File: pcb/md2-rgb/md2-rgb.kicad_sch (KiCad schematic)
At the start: 19 parts, among them J101 MD-90SM, J102 MD-90SM

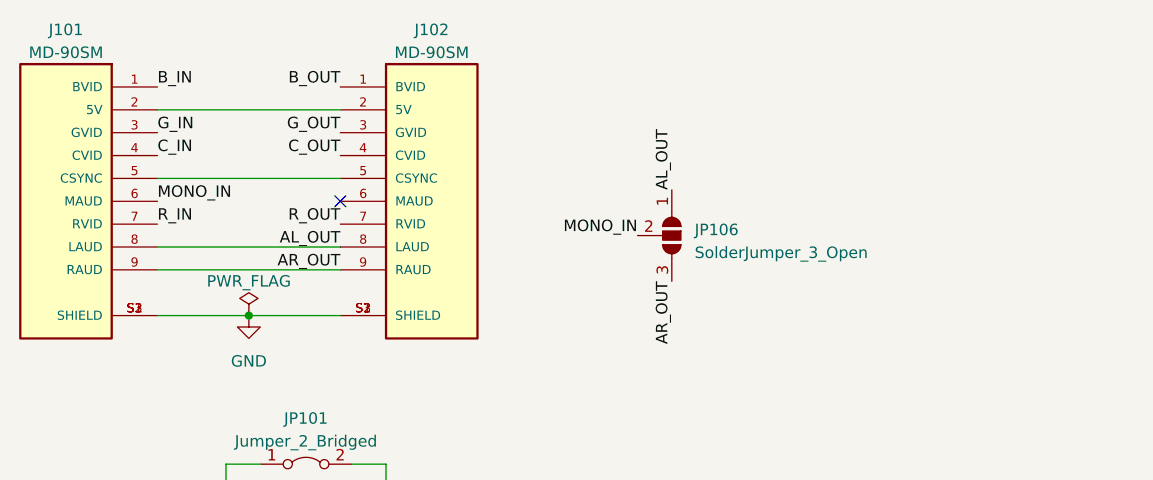
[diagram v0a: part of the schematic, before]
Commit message: Adds FPC to RGB breakout
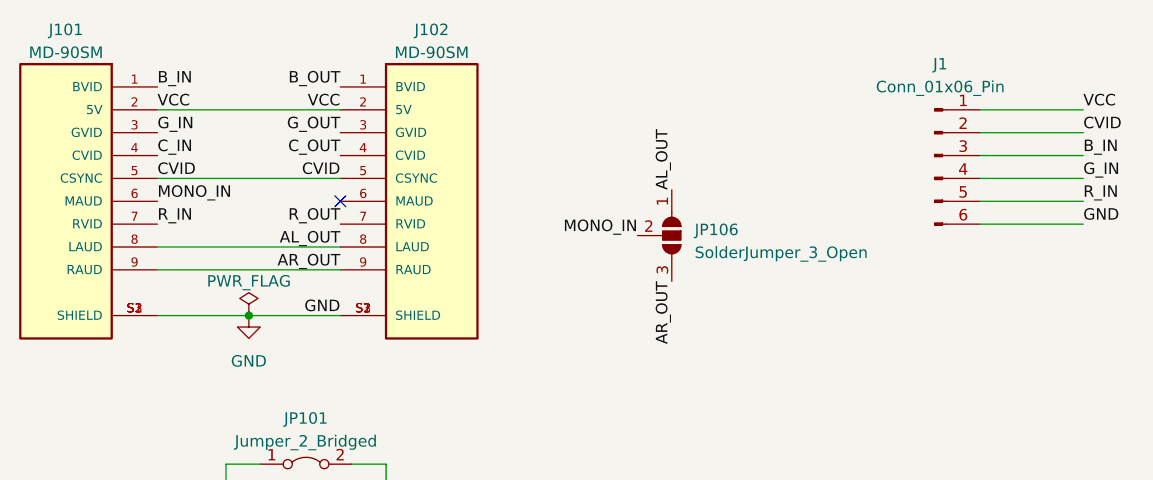
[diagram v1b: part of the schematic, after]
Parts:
- added J1: Conn_01x06_Pin, Connector_FFC-FPC:TE_0-1734839-6_1x06-1MP_P0.5mm_Horizontal, symbol Connector:Conn_01x06_Pin
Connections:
- net B_IN: now also J1.3 (Pin_3)
- net GND: now also J1.6 (Pin_6)
- net G_IN: now also J1.4 (Pin_4)
- net R_IN: now also J1.5 (Pin_5)
- net VCC: now reaches J101.2 (5V), J102.2 (5V)
- net VCC: now also J1.1 (Pin_1)
- net CVID: now reaches J101.5 (CSYNC), J102.5 (CSYNC)
- net CVID: now also J1.2 (Pin_2)
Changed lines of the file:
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@@
+    (stroke (width 0) (type default))
+  )
+  (wire (pts (xy 143.51 30.48) (xy 132.08 30.48))
+    (stroke (width 0) (type default))
+  )
+  (wire (pts (xy 143.51 38.1) (xy 132.08 38.1))
     (stroke (width 0) (type default))
   )
@@
     (stroke (width 0) (type default))
   )
+  (wire (pts (xy 143.51 43.18) (xy 132.08 43.18))
+    (stroke (width 0) (type default))
+  )
   (wire (pts (xy 62.23 134.62) (xy 66.04 134.62))
     (stroke (width 0) (type default))
   )
+  (wire (pts (xy 143.51 35.56) (xy 132.08 35.56))
+    (stroke (width 0) (type default))
+  )
   (wire (pts (xy 66.04 175.26) (xy 71.12 175.26))
     (stroke (width 0) (type default))
@@
     (stroke (width 0) (type default))
   )
+  (wire (pts (xy 143.51 33.02) (xy 132.08 33.02))
+    (stroke (width 0) (type default))
+  )
   (wire (pts (xy 48.26 110.49) (xy 50.8 110.49))
     (stroke (width 0) (type default))
@@
     (stroke (width 0) (type default))
   )
+  (wire (pts (xy 143.51 40.64) (xy 132.08 40.64))
+    (stroke (width 0) (type default))
+  )
   (wire (pts (xy 48.26 78.74) (xy 48.26 69.85))
     (stroke (width 0) (type default))
@@
     (effects (font (size 1.27 1.27)) (justify left bottom))
   )
+  (label "GND" (at 60.96 53.34 180) (fields_autoplaced)
+    (effects (font (size 1.27 1.27)) (justify right bottom))
+  )
   (label "AR_OUT" (at 97.79 49.53 270) (fields_autoplaced)
     (effects (font (size 1.27 1.27)) (justify right bottom))
   )
+  (label "VCC" (at 60.96 30.48 180) (fields_autoplaced)
+    (effects (font (size 1.27 1.27)) (justify right bottom))
+  )
   (label "B_IN" (at 44.45 143.51 180) (fields_autoplaced)
     (effects (font (size 1.27 1.27)) (justify right bottom))
@@
     (effects (font (size 1.27 1.27)) (justify right bottom))
   )
+  (label "B_IN" (at 143.51 35.56 0) (fields_autoplaced)
+    (effects (font (size 1.27 1.27)) (justify left bottom))
+  )
   (label "R_IN" (at 44.45 78.74 180) (fields_autoplaced)
     (effects (font (size 1.27 1.27)) (justify right bottom))
@@
     (effects (font (size 1.27 1.27)) (justify right bottom))
   )
+  (label "VCC" (at 143.51 30.48 0) (fields_autoplaced)
+    (effects (font (size 1.27 1.27)) (justify left bottom))
+  )
   (label "G_IN" (at 44.45 110.49 180) (fields_autoplaced)
     (effects (font (size 1.27 1.27)) (justify right bottom))
   )
+  (label "R_IN" (at 143.51 40.64 0) (fields_autoplaced)
+    (effects (font (size 1.27 1.27)) (justify left bottom))
+  )
   (label "MONO_IN" (at 40.64 40.64 0) (fields_autoplaced)
     (effects (font (size 1.27 1.27)) (justify left bottom))
@@
     (effects (font (size 1.27 1.27)) (justify left bottom))
   )
+  (label "CVID" (at 60.96 38.1 180) (fields_autoplaced)
+    (effects (font (size 1.27 1.27)) (justify right bottom))
+  )
   (label "G_OUT" (at 71.12 110.49 0) (fields_autoplaced)
     (effects (font (size 1.27 1.27)) (justify left bottom))
@@
     (effects (font (size 1.27 1.27)) (justify left bottom))
   )
+  (label "CVID" (at 40.64 38.1 0) (fields_autoplaced)
+    (effects (font (size 1.27 1.27)) (justify left bottom))
+  )
   (label "B_OUT" (at 60.96 27.94 180) (fields_autoplaced)
     (effects (font (size 1.27 1.27)) (justify right bottom))
   )
+  (label "GND" (at 143.51 43.18 0) (fields_autoplaced)
+    (effects (font (size 1.27 1.27)) (justify left bottom))
+  )
+  (label "CVID" (at 143.51 33.02 0) (fields_autoplaced)
+    (effects (font (size 1.27 1.27)) (justify left bottom))
+  )
+  (label "G_IN" (at 143.51 38.1 0) (fields_autoplaced)
+    (effects (font (size 1.27 1.27)) (justify left bottom))
+  )
   (label "C_OUT" (at 60.96 35.56 180) (fields_autoplaced)
     (effects (font (size 1.27 1.27)) (justify right bottom))
+  )
+  (label "VCC" (at 40.64 30.48 0) (fields_autoplaced)
+    (effects (font (size 1.27 1.27)) (justify left bottom))
   )
   (label "R_OUT" (at 60.96 43.18 180) (fields_autoplaced)
@@
         )
       )
+    )
+  )
+  (symbol (lib_id "Connector:Conn_01x06_Pin") (at 127 35.56 0) (unit 1)
+    (in_bom yes) (on_board yes) (dnp no) (fields_autoplaced)
+    (property "Reference" "J1" (at 127.635 25.4 0)
+      (effects (font (size 1.27 1.27)))
+    )
+    (property "Value" "Conn_01x06_Pin" (at 127.635 27.94 0)
+      (effects (font (size 1.27 1.27)))
+    )
+    (property "Footprint" "Connector_FFC-FPC:TE_0-1734839-6_1x06-1MP_P0.5mm_Horizontal" (at 127 35.56 0)
+      (effects (font (size 1.27 1.27)) hide)
+    )
+    (property "Datasheet" "~" (at 127 35.56 0)
+      (effects (font (size 1.27 1.27)) hide)
+    )
+    (pin "1")
+    (pin "2")
+    (pin "3")
+    (pin "4")
+    (pin "5")
+    (pin "6")
+    (instances
+      (project "md2-rgb"
+        (path "/8135f8d6-ea78-471e-a120-e2dd0a7eef29"
+          (reference "J1") (unit 1)
+        )
+      )

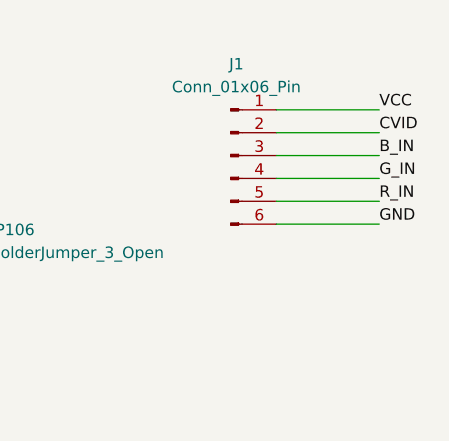
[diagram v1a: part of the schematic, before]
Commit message: Flips FFC
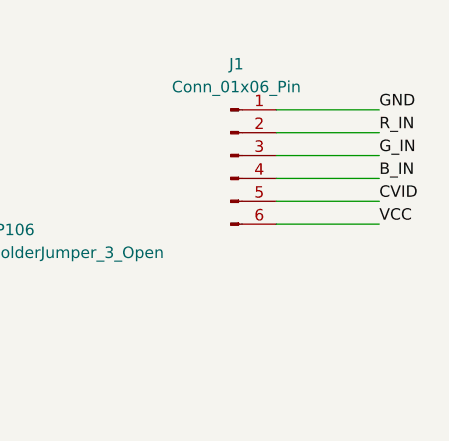
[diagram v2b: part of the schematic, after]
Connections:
- net B_IN: now also J1.4 (Pin_4); no longer J1.3 (Pin_3)
- net CVID: now also J1.5 (Pin_5); no longer J1.2 (Pin_2)
- net GND: now also J1.1 (Pin_1); no longer J1.6 (Pin_6)
- net G_IN: now also J1.3 (Pin_3); no longer J1.4 (Pin_4)
- net R_IN: now also J1.2 (Pin_2); no longer J1.5 (Pin_5)
- net VCC: now also J1.6 (Pin_6); no longer J1.1 (Pin_1)
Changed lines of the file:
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@@
     (effects (font (size 1.27 1.27)) (justify right bottom))
   )
-  (label "B_IN" (at 143.51 35.56 0) (fields_autoplaced)
+  (label "B_IN" (at 143.51 38.1 0) (fields_autoplaced)
     (effects (font (size 1.27 1.27)) (justify left bottom))
   )
@@
     (effects (font (size 1.27 1.27)) (justify right bottom))
   )
-  (label "VCC" (at 143.51 30.48 0) (fields_autoplaced)
+  (label "VCC" (at 143.51 43.18 0) (fields_autoplaced)
     (effects (font (size 1.27 1.27)) (justify left bottom))
   )
@@
     (effects (font (size 1.27 1.27)) (justify right bottom))
   )
-  (label "R_IN" (at 143.51 40.64 0) (fields_autoplaced)
+  (label "R_IN" (at 143.51 33.02 0) (fields_autoplaced)
     (effects (font (size 1.27 1.27)) (justify left bottom))
   )
@@
     (effects (font (size 1.27 1.27)) (justify right bottom))
   )
-  (label "GND" (at 143.51 43.18 0) (fields_autoplaced)
-    (effects (font (size 1.27 1.27)) (justify left bottom))
-  )
-  (label "CVID" (at 143.51 33.02 0) (fields_autoplaced)
-    (effects (font (size 1.27 1.27)) (justify left bottom))
-  )
-  (label "G_IN" (at 143.51 38.1 0) (fields_autoplaced)
+  (label "GND" (at 143.51 30.48 0) (fields_autoplaced)
+    (effects (font (size 1.27 1.27)) (justify left bottom))
+  )
+  (label "CVID" (at 143.51 40.64 0) (fields_autoplaced)
+    (effects (font (size 1.27 1.27)) (justify left bottom))
+  )
+  (label "G_IN" (at 143.51 35.56 0) (fields_autoplaced)
     (effects (font (size 1.27 1.27)) (justify left bottom))
   )
@@
     )
   )
-  (symbol (lib_id "Connector:Conn_01x06_Pin") (at 127 35.56 0) (unit 1)
-    (in_bom yes) (on_board yes) (dnp no) (fields_autoplaced)
-    (property "Reference" "J1" (at 127.635 25.4 0)
-      (effects (font (size 1.27 1.27)))
-    )
-    (property "Value" "Conn_01x06_Pin" (at 127.635 27.94 0)
-      (effects (font (size 1.27 1.27)))
-    )
-    (property "Footprint" "Connector_FFC-FPC:TE_0-1734839-6_1x06-1MP_P0.5mm_Horizontal" (at 127 35.56 0)
-      (effects (font (size 1.27 1.27)) hide)
-    )
-    (property "Datasheet" "~" (at 127 35.56 0)
-      (effects (font (size 1.27 1.27)) hide)
-    )
-    (pin "1")
-    (pin "2")
-    (pin "3")
-    (pin "4")
-    (pin "5")
-    (pin "6")
-    (instances
-      (project "md2-rgb"
-        (path "/8135f8d6-ea78-471e-a120-e2dd0a7eef29"
-          (reference "J1") (unit 1)
-        )
-      )
-    )
-  )
   (symbol (lib_id "Device:R_Small") (at 60.96 83.82 270) (unit 1)
     (in_bom yes) (on_board yes) (dnp no) (fields_autoplaced)
@@
         )
       )
+    )
+  )
+  (symbol (lib_id "Connector:Conn_01x06_Pin") (at 127 35.56 0) (unit 1)
+    (in_bom yes) (on_board yes) (dnp no)
+    (property "Reference" "J1" (at 127.635 25.4 0)
+      (effects (font (size 1.27 1.27)))
+    )
+    (property "Value" "Conn_01x06_Pin" (at 127.635 27.94 0)
+      (effects (font (size 1.27 1.27)))
+    )
+    (property "Footprint" "Connector_FFC-FPC:TE_0-1734839-6_1x06-1MP_P0.5mm_Horizontal" (at 127 35.56 0)
+      (effects (font (size 1.27 1.27)) hide)
+    )
+    (property "Datasheet" "~" (at 127 35.56 0)
+      (effects (font (size 1.27 1.27)) hide)
+    )
+    (pin "1")
+    (pin "2")
+    (pin "3")
+    (pin "4")
+    (pin "5")
+    (pin "6")
+    (instances
+      (project "md2-rgb"
+        (path "/8135f8d6-ea78-471e-a120-e2dd0a7eef29"
+          (reference "J1") (unit 1)
+        )
+      )

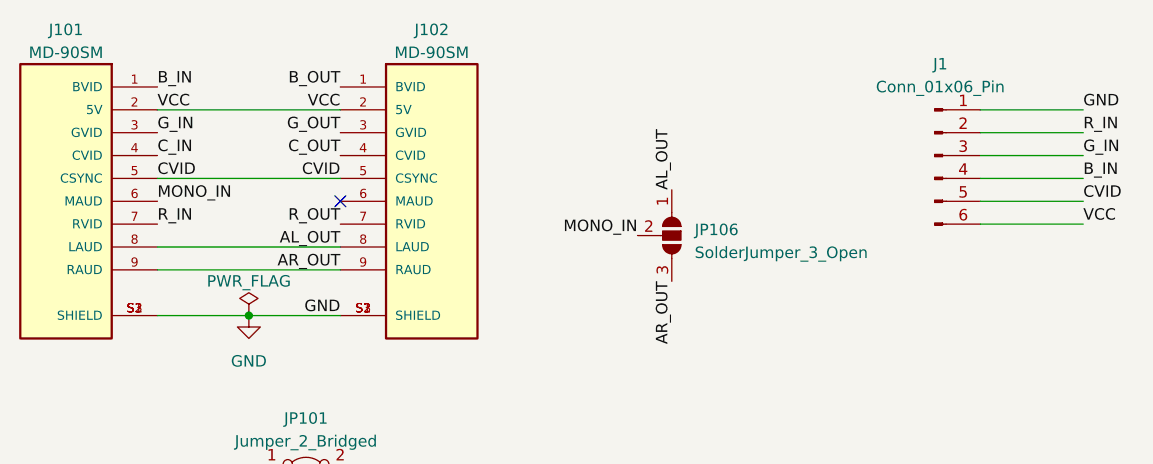
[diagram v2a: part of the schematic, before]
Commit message: connects FFC to composite in, not sync
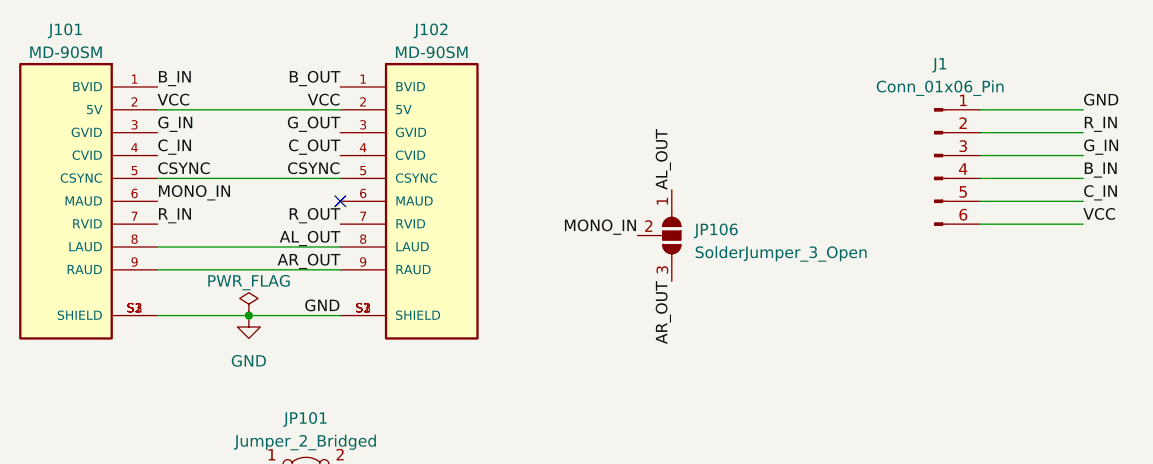
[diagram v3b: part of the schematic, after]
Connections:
- net C_IN: now also J1.5 (Pin_5)
- net CVID renamed CSYNC
- net CSYNC: no longer J1.5 (Pin_5)
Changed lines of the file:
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@@
     (effects (font (size 1.27 1.27)) (justify left bottom))
   )
-  (label "CVID" (at 60.96 38.1 180) (fields_autoplaced)
+  (label "CSYNC" (at 60.96 38.1 180) (fields_autoplaced)
     (effects (font (size 1.27 1.27)) (justify right bottom))
   )
@@
     (effects (font (size 1.27 1.27)) (justify left bottom))
   )
-  (label "CVID" (at 40.64 38.1 0) (fields_autoplaced)
+  (label "CSYNC" (at 40.64 38.1 0) (fields_autoplaced)
     (effects (font (size 1.27 1.27)) (justify left bottom))
   )
@@
     (effects (font (size 1.27 1.27)) (justify left bottom))
   )
-  (label "CVID" (at 143.51 40.64 0) (fields_autoplaced)
+  (label "C_IN" (at 143.51 40.64 0) (fields_autoplaced)
     (effects (font (size 1.27 1.27)) (justify left bottom))
   )
